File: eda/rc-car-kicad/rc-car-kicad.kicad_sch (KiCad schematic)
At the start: 59 parts, among them J1 Servo Sig, J10 RF 3.3V, J11 RF CE, J12 RF CSN, J13 RF SCK, J14 RF MOSI, J15 RF MISO, J16 Gnd, J17 3.3V, J18 8.2V, J19 Battery, J2 Servo Gnd, J20 8.2V, J3 Servo 5V, J4 DC Motor -, J5 DC Motor +, J6 ISP RESET, J7 3.3V, J8 Gnd, J9 RF Gnd, Q1 IRLML6244, Q2 IRLML2246, Q3 IRLML2246, Q4 IRLML6244, Q5 MMBT3904, Q6 MMBT3904, SW1 SW_SPST, U1 TPS3840, U2 MIC5225-3.3YM5, U3 ATmega164A-A, U4 MIC3975-5.0YMM

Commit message: - Updated the panel pcb and schematic - Added a boost functionality - Removed unnecessary usart code - Movied analog reading code into the joystick class
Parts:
- R11: value 953k -> 470k
- R12: value 1M -> 500k
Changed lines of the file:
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@@
 			)
 		)
-		(property "Value" "1M"
+		(property "Value" "500k"
 			(at 60.96 63.4999 0)
 			(effects
@@
 			)
 		)
-		(property "Value" "953k"
+		(property "Value" "470k"
 			(at 60.96 50.7999 0)
 			(effects

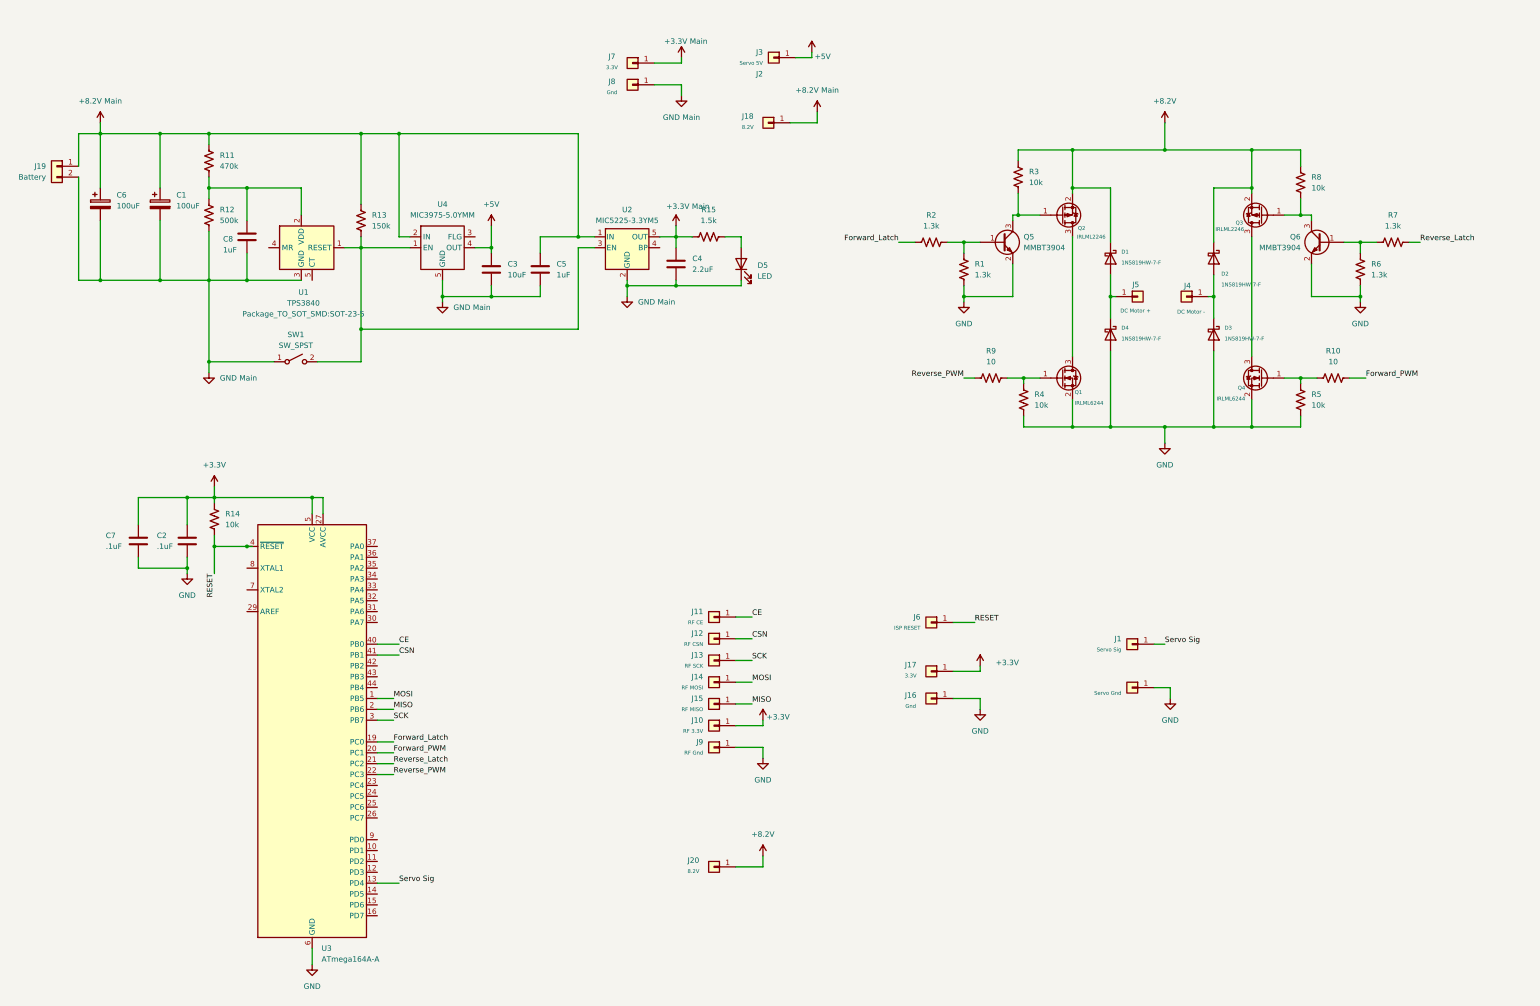
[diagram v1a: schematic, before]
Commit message: - Redesigned power portion of the pcb - Changed the board to atmega164A
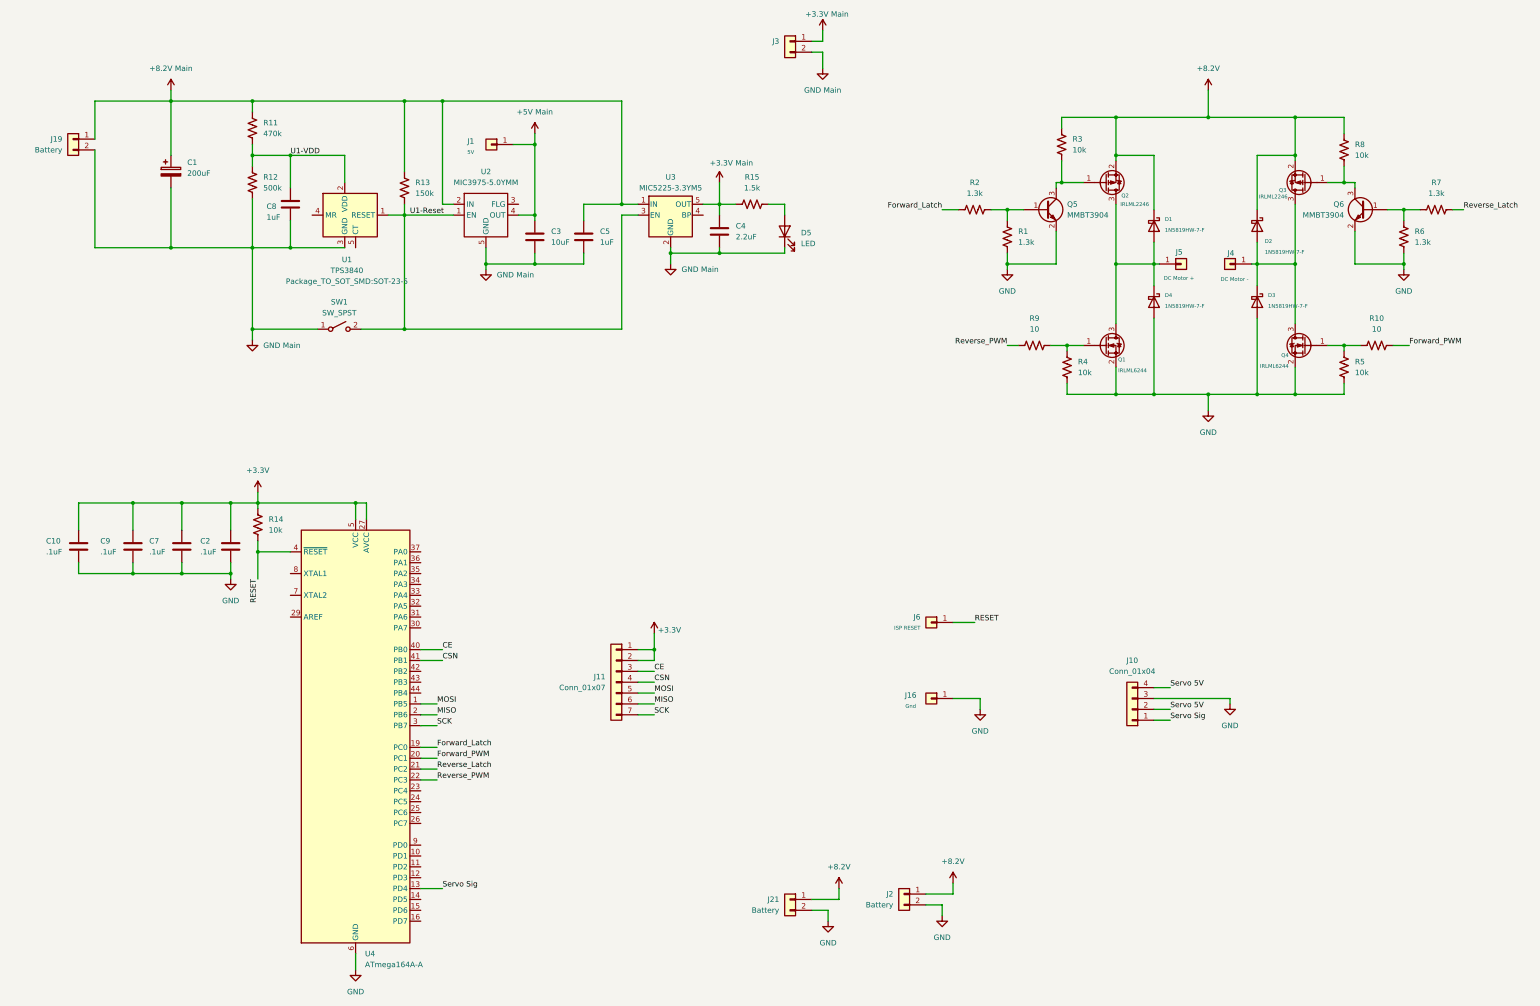
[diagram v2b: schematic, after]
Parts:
- removed C1: 100uF, Capacitor_THT:CP_Radial_D6.3mm_P2.50mm, symbol Device:C_Polarized
- removed J10: RF 3.3V, Connector_PinHeader_2.54mm:PinHeader_1x01_P2.54mm_Vertical, symbol Connector_Generic:Conn_01x01
- removed J11: RF CE, Connector_PinHeader_2.54mm:PinHeader_1x01_P2.54mm_Vertical, symbol Connector_Generic:Conn_01x01
- removed J12: RF CSN, Connector_PinHeader_2.54mm:PinHeader_1x01_P2.54mm_Vertical, symbol Connector_Generic:Conn_01x01
- removed J13: RF SCK, Connector_PinHeader_2.54mm:PinHeader_1x01_P2.54mm_Vertical, symbol Connector_Generic:Conn_01x01
- removed J14: RF MOSI, Connector_PinHeader_2.54mm:PinHeader_1x01_P2.54mm_Vertical, symbol Connector_Generic:Conn_01x01
- removed J15: RF MISO, Connector_PinHeader_2.54mm:PinHeader_1x01_P2.54mm_Vertical, symbol Connector_Generic:Conn_01x01
- removed J17, J7: 3.3V, Connector_PinHeader_2.54mm:PinHeader_1x01_P2.54mm_Vertical, symbol Connector_Generic:Conn_01x01
- removed J18, J20: 8.2V, Connector_PinHeader_2.54mm:PinHeader_1x01_P2.54mm_Vertical, symbol Connector_Generic:Conn_01x01
- removed J2: Servo Gnd, Connector_PinHeader_2.54mm:PinHeader_1x01_P2.54mm_Vertical, symbol Connector_Generic:Conn_01x01
- removed J3: Servo 5V, Connector_PinHeader_2.54mm:PinHeader_1x01_P2.54mm_Vertical, symbol Connector_Generic:Conn_01x01
- removed J8: Gnd, Connector_PinHeader_2.54mm:PinHeader_1x01_P2.54mm_Vertical, symbol Connector_Generic:Conn_01x01
- removed J9: RF Gnd, Connector_PinHeader_2.54mm:PinHeader_1x01_P2.54mm_Vertical, symbol Connector_Generic:Conn_01x01
- added C10, C9: .1uF, Capacitor_SMD:C_0603_1608Metric_Pad1.08x0.95mm_HandSolder, symbol Device:C
- added J10: Conn_01x04, Connector_PinHeader_2.54mm:PinHeader_1x04_P2.54mm_Vertical, symbol Connector_Generic:Conn_01x04
- added J11: Conn_01x07, Connector_PinHeader_2.54mm:PinHeader_1x07_P2.54mm_Vertical, symbol Connector_Generic:Conn_01x07
- added J2, J21: Battery, Connector_PinHeader_2.54mm:PinHeader_1x02_P2.54mm_Vertical, symbol Connector_Generic:Conn_01x02
- added J3: (no value), Connector_PinSocket_2.54mm:PinSocket_1x02_P2.54mm_Vertical, symbol Connector_Generic:Conn_01x02
- C1: renamed from C6; value 100uF -> 200uF; footprint Capacitor_THT:CP_Radial_D6.3mm_P2.50mm -> Capacitor_THT:CP_Radial_D8.0mm_P3.50mm
- J1: value Servo Sig -> 5V; footprint Connector_PinHeader_2.54mm:PinHeader_1x01_P2.54mm_Vertical -> Connector_PinSocket_2.54mm:PinSocket_1x01_P2.54mm_Vertical
- J19: footprint Connector_PinHeader_2.54mm:PinHeader_1x02_P2.54mm_Vertical -> Connector_PinSocket_2.54mm:PinSocket_1x02_P2.54mm_Vertical
- J6: footprint Connector_PinHeader_2.54mm:PinHeader_1x01_P2.54mm_Vertical -> TestPoint:TestPoint_Pad_1.0x1.0mm
- renumbered U4 to U2, U2 to U3, U3 to U4
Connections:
- net +3.3V: now also C10.1, C9.1, J11.1 (Pin_1), J11.2 (Pin_2)
- net +3.3V Main: now also J3.1 (Pin_1)
- net +8.2V: now also J2.1 (Pin_1), J21.1 (Pin_1)
- net CE: now also J11.3 (Pin_3)
- net CSN: now also J11.4 (Pin_4)
- net GND: now also C10.2, C9.2, J10.3 (Pin_3), J2.2 (Pin_2), J21.2 (Pin_2)
- net GND Main: now also J3.2 (Pin_2)
- net MISO: now also J11.6 (Pin_6)
- net MOSI: now also J11.5 (Pin_5)
- net SCK: now also J11.7 (Pin_7)
- net Servo Sig: now also J10.1 (Pin_1); no longer J1.1 (Pin_1)
- net U1-Reset: now reaches R13.2, SW1.2 (B), U1.1 (RESET), U2.1 (EN), U3.3 (EN)
- net at D1.2 (A), D4.1 (K), J5.1 (Pin_1): now also Q1.3 (D), Q2.3 (D)
- net at D2.2 (A), D3.1 (K), J4.1 (Pin_1): now also Q3.3 (D), Q4.3 (D)
- net U1-VDD: now reaches C8.1, R11.2, R12.1, U1.2 (VDD)
- net +5V renamed +5V Main
- net +5V Main: now also J1.1 (Pin_1)
- new net Servo 5V: J10.2 (Pin_2), J10.4 (Pin_4)
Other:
- moved on the sheet: C1, C2, C3, C4, C5, C7, C8, D1, D2, D3, D4, D5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

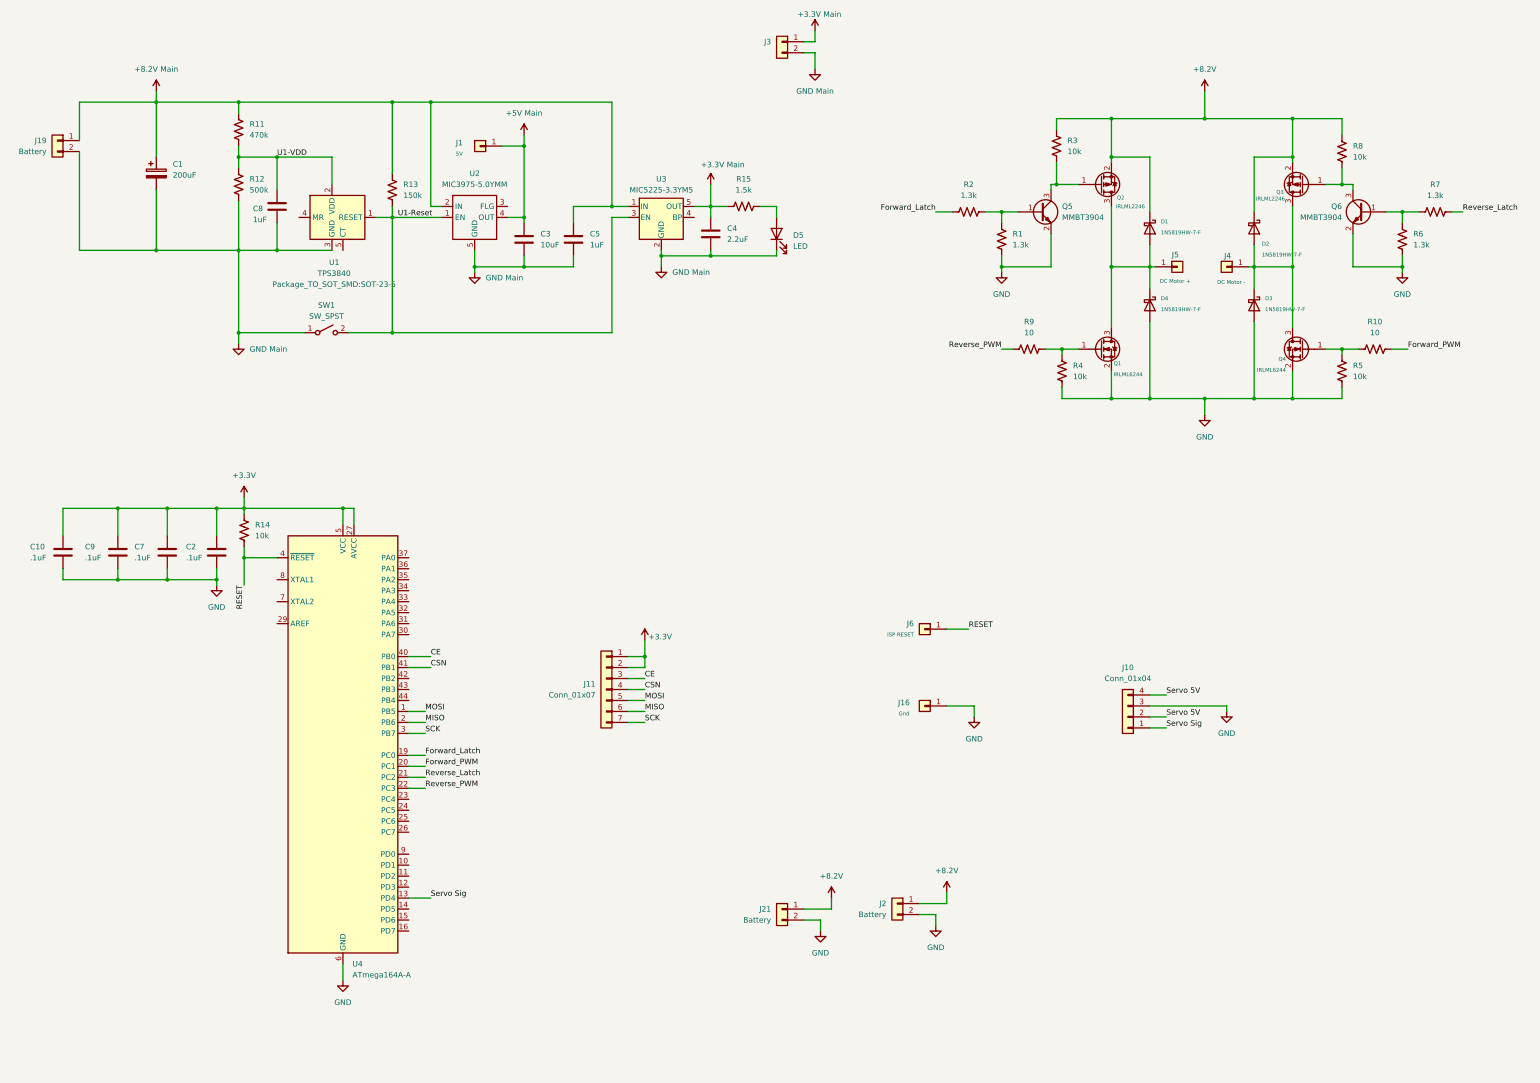
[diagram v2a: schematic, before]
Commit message: - Made improvements to power and ground plains on the powere pcb - Updated the component labels in the schematic
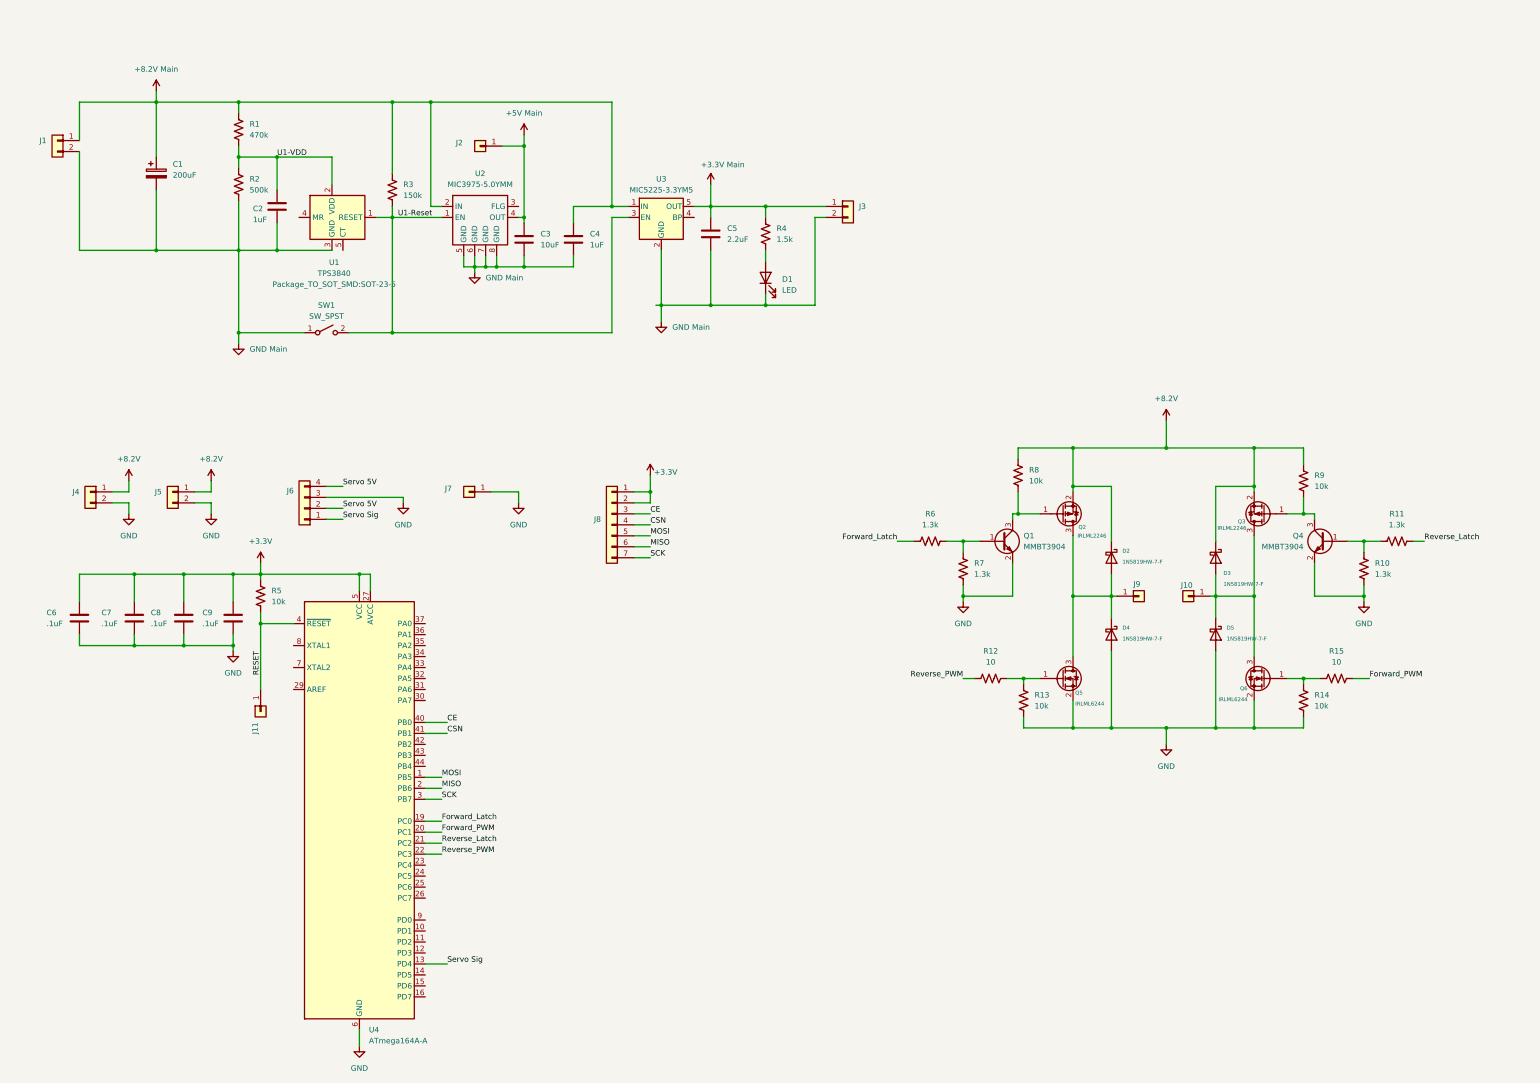
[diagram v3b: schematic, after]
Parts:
- J1: renamed from J19; value Battery -> ~
- J10: renamed from J4; value DC Motor - -> ~
- J11: renamed from J6; value ISP RESET -> ~
- J2: renamed from J1; value 5V -> ~
- J3: value (none) -> ~
- J4: renamed from J21; value Battery -> ~
- J5: renamed from J2; value Battery -> ~
- J6: renamed from J10; value Conn_01x04 -> ~
- J7: renamed from J16; value Gnd -> ~
- J8: renamed from J11; value Conn_01x07 -> ~
- J9: renamed from J5; value DC Motor + -> ~
- renumbered C8 to C2, C5 to C4, C4 to C5, C10 to C6, C9 to C7, C7 to C8, C2 to C9, D5 to D1, D1 to D2, D2 to D3, D3 to D5, Q5 to Q1, Q6 to Q4, Q1 to Q5, Q4 to Q6, R11 to R1, R6 to R10, R7 to R11, R9 to R12, R4 to R13, R5 to R14, R10 to R15, R12 to R2, R13 to R3, R15 to R4, R14 to R5, R2 to R6, R1 to R7, R3 to R8, R8 to R9
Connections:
- net +3.3V Main: now also R4.2; no longer R4.1
- net GND Main: now also U2.6 (GND), U2.7 (GND), U2.8 (GND)
- net at D1.2 (A): now also R4.1; no longer R4.2
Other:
- moved on the sheet: C6, C7, C8, C9, D1, D2, D3, D4, D5, J10, J11, J3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

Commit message: - Added testing points for H-Bridge connections to the PCB
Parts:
- added J12, J13, J14, J15: (no value), TestPoint:TestPoint_Pad_D1.0mm, symbol Connector_Generic:Conn_01x01
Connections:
- net Forward_Latch: now also J12.1 (Pin_1)
- net Forward_PWM: now also J13.1 (Pin_1)
- net Reverse_Latch: now also J14.1 (Pin_1)
- net Reverse_PWM: now also J15.1 (Pin_1)
